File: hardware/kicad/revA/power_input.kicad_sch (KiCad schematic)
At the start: 0 parts

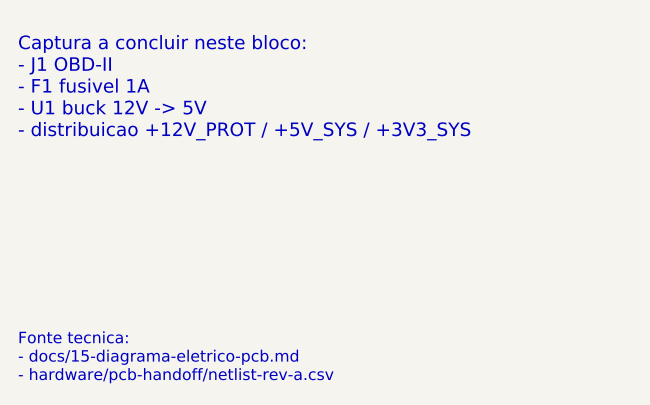
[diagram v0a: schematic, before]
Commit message: Align RevA pinout and retire legacy handoff
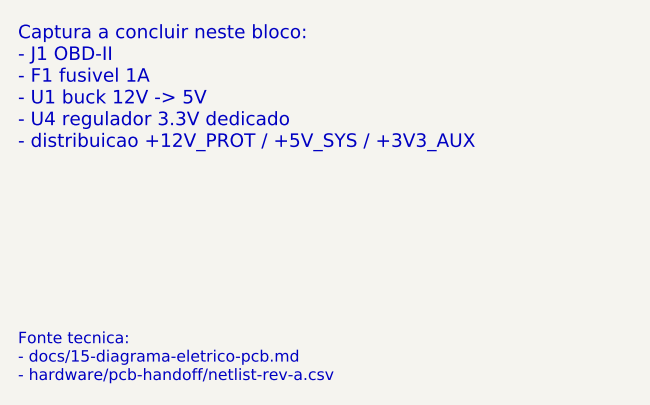
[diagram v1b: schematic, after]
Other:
- note added: "Captura a concluir neste bloco: - J1 OBD-II - F1 fusivel 1A - U1 buck 12V -> 5V - U4 regulador 3.3V dedicado - distribuicao +12V_PROT / +5V_SYS / +3V3_AUX"
- note removed: "Captura a concluir neste bloco: - J1 OBD-II - F1 fusivel 1A - U1 buck 12V -> 5V - distribuicao +12V_PROT / +5V_SYS / +3V3_SYS"
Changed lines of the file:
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@@
 		(comment 2 "J1 pin4/pin5 -> GND comum")
 	)
-	(text "Captura a concluir neste bloco:\n- J1 OBD-II\n- F1 fusivel 1A\n- U1 buck 12V -> 5V\n- distribuicao +12V_PROT / +5V_SYS / +3V3_SYS"
+	(text "Captura a concluir neste bloco:\n- J1 OBD-II\n- F1 fusivel 1A\n- U1 buck 12V -> 5V\n- U4 regulador 3.3V dedicado\n- distribuicao +12V_PROT / +5V_SYS / +3V3_AUX"
 		(exclude_from_sim no)
 		(at 18 22 0)

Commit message: Consolidate docs set and finalize Wi-Fi config updates
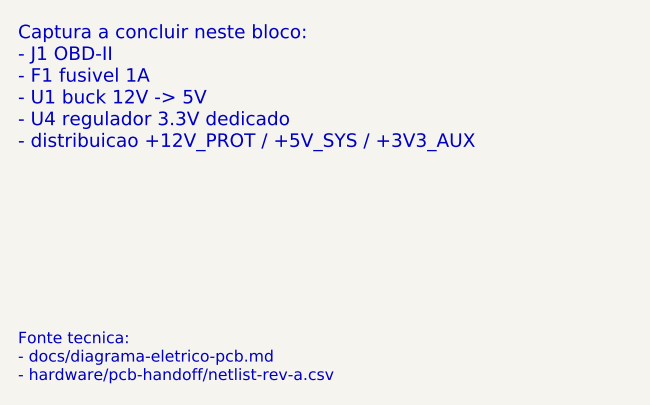
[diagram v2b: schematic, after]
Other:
- note added: "Fonte tecnica: - docs/diagrama-eletrico-pcb.md - hardware/pcb-handoff/netlist-rev-a.csv"
- note removed: "Fonte tecnica: - docs/15-diagrama-eletrico-pcb.md - hardware/pcb-handoff/netlist-rev-a.csv"
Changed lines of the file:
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@@
 		)
 	)
-	(text "Fonte tecnica:\n- docs/15-diagrama-eletrico-pcb.md\n- hardware/pcb-handoff/netlist-rev-a.csv"
+(text "Fonte tecnica:\n- docs/diagrama-eletrico-pcb.md\n- hardware/pcb-handoff/netlist-rev-a.csv"
 		(exclude_from_sim no)
 		(at 18 52 0)
